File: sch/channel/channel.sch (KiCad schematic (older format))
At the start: 92 parts, among them IC1 STM32F030F4, IC2 L200, IC3 TL072, IC4 LM2594, IC5 TL074, IC6 LM2594, IC7 OPTO_COUPLER, IC8 MCP1700-3002E/TT, P1 CONN_2, P10 CONN_3, P11 CONN_6, P12 CONN_1, P13 CONN_2, P14 CONN_1, P15 CONN_1, P16 CONN_1, P17 CONN_1, P18 CONN_1, P19 CONN_5, P2 CONN_3, P3 DC_JACK, P4 CONN_1, P5 CONN_1, P6 CONN_3, P7 CONN_5, P8 CONN_1, P9 CONN_1, Q1 2N3904, Q2 2N3904, SW1 SWITCH_INV_MECH, SW2 SWITCH_INV_MECH, U1 LM7812

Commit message: Started assigning footprints for components
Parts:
- added C16, C18: 4.7uF, symbol C
- added C17: 1uF, symbol C
- added C19, C20: 100nF, symbol C
- added IC10: 74HCT125, symbol 74HCT125
- added IC9: MCP1824ST-3302E, symbol MCP1824ST-3302E
- added P20, P21: CONN_3, symbol CONN_3
- added P22, P23, P24, P25: CONN_1, symbol CONN_1
- C13: value C -> 100nF
- C7: value C -> 10nF
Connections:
- net +3.3V: now also C17.1, C18.1, IC9.3 (Vout), P20.1 (P1), P21.1 (P1); no longer C10.1, IC6.4 (FB), L2.2, P19.1
- net GND: now also C16.2, C17.2, C18.2, C19.2, IC10.1 (E), IC10.10 (E), IC10.12 (D), IC10.13 (E), IC10.4 (E), IC10.7 (GND), IC10.7 (GND), IC10.7 (GND), IC10.7 (GND), IC9.2 (GND), IC9.4 (GND)
- net ICUR_MEAS: now also C20.1
- net LOAD: now also IC10.2 (D); no longer P19.2
- net SCK: now also IC10.5 (D); no longer P19.3
- net SDO: now also IC10.9 (D); no longer P19.4
- net at IC5.12 (+), R26.2, RV5.1: now also C19.1
- net at IC5.13 (-), R25.2, R28.1: now also C20.2
- new net: P19.1, P21.2 (PM)
- new net: IC10.3 (O), P19.2
- new net: IC10.6 (O), P19.3
- new net: IC10.8 (O), P19.4
- new net +5V: C10.1, C16.1, IC6.4 (FB), IC9.1 (Vin), L2.2, P20.3 (P3), P21.3 (P3)
- new net VCC: IC10.14 (VCC), IC10.14 (VCC), IC10.14 (VCC), IC10.14 (VCC), P20.2 (PM)
- no-connect marks 16 -> 22
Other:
- moved on the sheet: P15, P16, P17, P18, P19

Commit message: Associating some more footprints
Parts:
- removed Q1, Q2: 2N3904, symbol 2N3904
- added Q1, Q2: BC817, symbol BC817
- C12, C14: value C -> 100nF
- C15: value CAPAPOL -> 10uF
- C9: value CAPAPOL -> 1000uF
- D4: value DIODE -> 1N4001
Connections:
- net GND: now also Q2.2 (E)
- net OUT_ON: now also Q2.3 (C)
- net at IC7.2 (K), P2.1 (P1): now also Q1.2 (E)
- net at D4.1 (A), JP7.1, RL1.1: now also Q1.3 (C)
- net at R30.2: now also Q1.1 (B)
- net at R11.1, R12.1: now also Q2.1 (B)
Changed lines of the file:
@@
 LIBS:valves
 LIBS:xilinx
+LIBS:channel-cache
 EELAYER 24 0
 EELAYER END
@@
 $EndComp
 $Comp
-L 2N3904 Q1
-U 1 1 52E5661F
-P 9450 4500
-F 0 "Q1" H 9550 4650 60  0000 C CNN
-F 1 "2N3904" H 9700 4300 60  0000 C CNN
-F 2 "" H 9450 4500 60  0000 C CNN
-F 3 "" H 9450 4500 60  0000 C CNN
-	1    9450 4500
-	-1   0    0    -1
-$EndComp
-$Comp
 L DIODE D4
 U 1 1 52E56633
 P 9000 4050
 F 0 "D4" H 9000 4150 40  0000 C CNN
-F 1 "DIODE" H 9000 3950 40  0000 C CNN
+F 1 "1N4001" H 9000 3950 40  0000 C CNN
 F 2 "" H 9000 4050 60  0000 C CNN
 F 3 "" H 9000 4050 60  0000 C CNN
@@
 P 5500 6550
 F 0 "C12" H 5550 6650 50  0000 L CNN
-F 1 "C" H 5550 6450 50  0000 L CNN
+F 1 "100nF" H 5550 6450 50  0000 L CNN
 F 2 "" H 5500 6550 60  0000 C CNN
 F 3 "" H 5500 6550 60  0000 C CNN
@@
 P 9100 6800
 F 0 "C14" H 9150 6900 50  0000 L CNN
-F 1 "C" H 9150 6700 50  0000 L CNN
+F 1 "100nF" H 9150 6700 50  0000 L CNN
 F 2 "" H 9100 6800 60  0000 C CNN
 F 3 "" H 9100 6800 60  0000 C CNN
@@
 P 10100 6800
 F 0 "C15" H 10150 6900 50  0000 L CNN
-F 1 "CAPAPOL" H 10150 6700 50  0000 L CNN
+F 1 "10uF" H 10150 6700 50  0000 L CNN
 F 2 "" H 10100 6800 60  0000 C CNN
 F 3 "" H 10100 6800 60  0000 C CNN
@@
 Wire Wire Line
 	10050 4050 10050 4150
-$Comp
-L 2N3904 Q2
-U 1 1 536919B5
-P 13200 6600
-F 0 "Q2" H 13300 6750 60  0000 C CNN
-F 1 "2N3904" H 13450 6400 60  0000 C CNN
-F 2 "" H 13200 6600 60  0000 C CNN
-F 3 "" H 13200 6600 60  0000 C CNN
-	1    13200 6600
-	-1   0    0    -1
-$EndComp
 Connection ~ 12050 6600
 Wire Wire Line
@@
 P 2450 1900
 F 0 "C9" H 2500 2000 50  0000 L CNN
-F 1 "CAPAPOL" H 2500 1800 50  0000 L CNN
+F 1 "1000uF" H 2500 1800 50  0000 L CNN
 F 2 "" H 2450 1900 60  0000 C CNN
 F 3 "" H 2450 1900 60  0000 C CNN
@@
 	1    0    0    -1
 $EndComp
+$Comp
+L BC817 Q1
+U 1 1 536C2B82
+P 9450 4500
+F 0 "Q1" H 9550 4650 60  0000 C CNN
+F 1 "BC817" H 9700 4300 60  0000 C CNN
+F 2 "" H 9450 4500 60  0000 C CNN
+F 3 "" H 9450 4500 60  0000 C CNN
+	1    9450 4500
+	-1   0    0    -1
+$EndComp
+$Comp
+L BC817 Q2
+U 1 1 536C363A
+P 13200 6600
+F 0 "Q2" H 13300 6750 60  0000 C CNN
+F 1 "BC817" H 13450 6400 60  0000 C CNN
+F 2 "" H 13200 6600 60  0000 C CNN
+F 3 "" H 13200 6600 60  0000 C CNN
+	1    13200 6600
+	-1   0    0    -1
+$EndComp
 $EndSCHEMATC

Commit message: Fully assigned components, changed the design to remove opto-coupler, using relay instead
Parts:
- removed C14: 100nF, symbol C
- removed C15: 10uF, symbol CAPAPOL
- removed IC7: OPTO_COUPLER, symbol OPTO_COUPLER
- removed Q2: BC817, symbol BC817
- removed R12, R31: 10k, symbol R
- removed R29: 330, symbol R
- removed RL1: RELAY, symbol RELAY
- removed SW2: SWITCH_INV_MECH, symbol SWITCH_INV_MECH
- removed U1: LM7812, symbol LM7812
- added JP11: JUMPER, symbol JUMPER
- added RL1: RELAY_DPDT, symbol RELAY_DPDT
- added SW2: DUAL_SWITCH_INV, symbol DUAL_SWITCH_INV
- L2: value 100uH -> 220uH
- R10: value 1k -> 180
- R11: value 1k -> 10k
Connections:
- net +3.3V: now also RL1.1NO
- net +5V: now also JP11.2
- net GND: now also RL1.1NC
- net OUT_ON: now also D9.1 (A), R11.2, RL1.1C; no longer IC1.9 (PA3/USART1_RX/ADC_IN3)
- net at C11.1, D5.2 (K), IC5.3 (+)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: now also RL1.2C
- net at P2.2 (PM), R30.1: now also SW2.2 (B)
- net at P2.1 (P1), Q1.2 (E): now also JP7.1
- net at D4.1 (A), Q1.3 (C): now also RL1.A1; no longer JP7.1
- net at D4.2 (K), P2.3 (P3): now also JP11.1, RL1.A2, SW2.3 (C); no longer D9.1 (A), R11.2
- net at P12.1, P13.1 (P1): now also RL1.2NO
- net at R11.1: now also IC1.9 (PA3/USART1_RX/ADC_IN3)
- no-connect marks 22 -> 23
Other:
- moved on the sheet: C1, C3, D4, D9, IC8, JP7, P12, P13, P14, P2, Q1, R10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

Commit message: Fully laid out PCB.  Needs a bit of tweaking for optimisation, and silk screen isn't done yet.
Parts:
- removed P20, P21: CONN_3, symbol CONN_3
- removed P22, P23, P24, P25: CONN_1, symbol CONN_1
- removed RV2, RV4: 10k, symbol POT
- added JP12, JP13, JP14, JP15, JP16, JP17: JUMPER, symbol JUMPER
- added RV2, RV4: 10k, symbol POT_MECH
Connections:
- net +3.0VA: now also RV2.3
- net +3.3V: now also RL1.2NO, JP14.2, JP16.2; no longer C1.1, IC8.3 (VIN), RL1.1NO
- net +5V: now also C1.1, IC8.3 (VIN), JP12.1, JP12.2, JP13.1, JP15.1
- net +VIN: now also JP17.2
- net GND: now also IC10.1 (E), IC10.10 (E), IC10.13 (E), IC10.2 (D), IC10.4 (E), P6.1 (P1), RL1.2NC, RV2.1, RV2.GND, RV4.GND; no longer IC10.1 (E), IC10.10 (E), IC10.12 (D), IC10.13 (E), IC10.4 (E), P6.3 (P3), RL1.1NC
- net LOAD: now also IC10.12 (D); no longer IC10.2 (D)
- net OUT_ON: now also RL1.2C; no longer RL1.1C
- net SCK: now also IC10.9 (D); no longer IC10.5 (D)
- net SDO: now also IC10.5 (D); no longer IC10.9 (D)
- net VCC: now also JP13.2, JP14.1
- net at C12.2, D7.2 (K), IC2.4 (REF)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: now also P6.3 (P3), RV4.1; no longer P6.2 (PM)
- net OUT_SENSE: now reaches IC2.5 (OUT), IC5.5 (+), JP3.1, JP3.2, R3.1, R5.1
- net OUT: now reaches C11.1, D5.2 (K), IC5.3 (+), JP6.1, JP6.2, R5.2, R7.1, RV1.3
- net OUT: now also RL1.1C; no longer RL1.2C
- net at RV1.2: now also P6.2 (PM), RV4.2; no longer P6.1 (P1)
- net NEG3V3IN: now reaches C4.1, C5.1, D1.2 (K), IC4.7 (VIN)
- net NEG3V3_SW: now reaches D2.2 (K), IC4.8 (OUT), L1.1
- net 5V_SW: now reaches D6.2 (K), IC6.8 (OUT), L2.1
- net A1: now reaches D4.1 (A), Q1.3 (C), RL1.A1
- net A2: now reaches D4.2 (K), JP11.1, P2.3 (P3), RL1.A2
- net A2: now also SW2.2 (B); no longer SW2.3 (C)
- net RELAY_GND: now reaches JP7.1, P2.1 (P1), Q1.2 (E)
- net at P2.2 (PM), R30.1: now also SW2.3 (C); no longer SW2.2 (B)
- net LED_PWR: now reaches P19.1
- net LED_PWR: now also JP15.2, JP16.1
- net at P19.2: now also IC10.11 (O); no longer IC10.3 (O)
- net at P19.3: now also IC10.8 (O); no longer IC10.6 (O)
- net at P19.4: now also IC10.6 (O); no longer IC10.8 (O)
- net VIN_SW: now reaches C9.1, JP5.1, P1.1 (P1), P3.1 (TIP), SW1.2
- net VIN_SW: now also JP17.1
- net SWITCHED_OUT: now reaches P12.1, P13.1 (P1)
- net SWITCHED_OUT: now also RL1.1NO; no longer RL1.2NO
- net at C12.1, IC3.2 (-), IC3.5 (+)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: now also RV2.2
- no-connect marks 23 -> 19
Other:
- note added: "0805 0Ohm link rated at 2A, so doubling up for safety"
- moved on the sheet: C1, C16, C17, C3, D4, IC8, IC9, JP10, JP11, JP7, JP8, JP9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

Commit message: A few tweaks to improve the layout.  Still not sorted silk screen.
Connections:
- net LOAD: now also IC1.14 (PB1/ADC_IN9); no longer IC1.10 (PA4/SPI1_NSS/USART1_CK/ADC_IN4)
- net at P8.1: now also IC1.10 (PA4/SPI1_NSS/USART1_CK/ADC_IN4); no longer IC1.14 (PB1/ADC_IN9)
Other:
- moved on the sheet: C7, JP2, P8, R1
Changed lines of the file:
@@
 Connection ~ 14000 4300
 Wire Wire Line
-	13400 4300 13200 4300
+	13200 4300 13400 4300
 Wire Wire Line
 	13300 4300 13300 4100
@@
 	12600 4300 12600 4100
 Wire Wire Line
-	12600 3700 12600 3450
+	12600 3450 12600 3700
 Wire Wire Line
 	12100 3450 12750 3450
@@
 Connection ~ 6950 2500
 Wire Wire Line
-	6500 1300 6000 1300
-Wire Wire Line
-	7000 1300 7850 1300
+	6000 1300 6500 1300
+Wire Wire Line
+	7850 1300 7000 1300
 Wire Wire Line
 	7850 700  7850 1900
@@
 Connection ~ 7700 2500
 Wire Wire Line
-	7100 2500 6800 2500
+	6800 2500 7100 2500
 Wire Wire Line
 	8100 1000 7850 1000
@@
 	3350 1200 5000 1200
 Wire Wire Line
-	14550 1650 14150 1650
+	14150 1650 14550 1650
 Wire Wire Line
 	14350 1800 14350 1650
@@
 	10200 3500 10300 3500
 Wire Wire Line
-	10300 3300 9300 3300
+	9300 3300 10300 3300
 Wire Wire Line
 	9400 4750 9400 4850
@@
 	7250 6400 7250 6600
 Wire Wire Line
-	7100 6850 6850 6850
+	6850 6850 7100 6850
 Wire Wire Line
 	6850 6550 6850 7150
@@
 Text Label 6100 10400 2    60   ~ 0
 SDO
-Text Label 2000 10600 0    60   ~ 0
+Text Label 6100 10300 2    60   ~ 0
 LOAD
 Wire Wire Line
@@
 	1500 9350 1500 9450
 Wire Wire Line
-	5700 10100 6550 10100
-Wire Wire Line
-	6550 10100 6550 9150
+	6550 10100 5700 10100
+Wire Wire Line
+	6550 9150 6550 10100
 Wire Wire Line
 	5700 10200 6550 10200
@@
 $EndComp
 Wire Wire Line
-	2300 10100 1000 10100
-Wire Wire Line
-	1000 9300 1000 10200
+	850  10100 2300 10100
+Wire Wire Line
+	850  9300 850  10200
 $Comp
 L C C7
 U 1 1 53685342
-P 1000 10400
-F 0 "C7" H 1050 10500 50  0000 L CNN
-F 1 "10nF" H 1050 10300 50  0000 L CNN
-F 2 "" H 1000 10400 60  0000 C CNN
-F 3 "" H 1000 10400 60  0000 C CNN
-	1    1000 10400
+P 850 10400
+F 0 "C7" H 900 10500 50  0000 L CNN
+F 1 "10nF" H 900 10300 50  0000 L CNN
+F 2 "" H 850 10400 60  0000 C CNN
+F 3 "" H 850 10400 60  0000 C CNN
+	1    850  10400
 	-1   0    0    -1
 $EndComp
 Wire Wire Line
-	1000 10600 1000 10700
-Connection ~ 1000 10100
+	850  10600 850  10700
+Connection ~ 850  10100
 $Comp
 L GND #PWR033
 U 1 1 536856E7
-P 1000 10700
-F 0 "#PWR033" H 1000 10700 30  0001 C CNN
-F 1 "GND" H 1000 10630 30  0001 C CNN
-F 2 "" H 1000 10700 60  0000 C CNN
-F 3 "" H 1000 10700 60  0000 C CNN
-	1    1000 10700
+P 850 10700
+F 0 "#PWR033" H 850 10700 30  0001 C CNN
+F 1 "GND" H 850 10630 30  0001 C CNN
+F 2 "" H 850 10700 60  0000 C CNN
+F 3 "" H 850 10700 60  0000 C CNN
+	1    850  10700
 	1    0    0    -1
 $EndComp
@@
 L +3.0VA #PWR034
 U 1 1 5368574A
-P 1000 9300
-F 0 "#PWR034" H 1000 9260 30  0001 C CNN
-F 1 "+3.0VA" H 1000 9410 30  0000 C CNN
-F 2 "" H 1000 9300 60  0000 C CNN
-F 3 "" H 1000 9300 60  0000 C CNN
-	1    1000 9300
+P 850 9300
+F 0 "#PWR034" H 850 9260 30  0001 C CNN
+F 1 "+3.0VA" H 850 9410 30  0000 C CNN
+F 2 "" H 850 9300 60  0000 C CNN
+F 3 "" H 850 9300 60  0000 C CNN
+	1    850  9300
 	1    0    0    -1
 $EndComp
@@
 $EndComp
 Wire Wire Line
-	2300 10000 1250 10000
-Wire Wire Line
-	1250 9900 1250 10200
-Connection ~ 1250 10000
+	1100 10000 2300 10000
+Wire Wire Line
+	1100 9900 1100 10200
+Connection ~ 1100 10000
 $Comp
 L JUMPER JP2
 U 1 1 5368ABD1
-P 1250 10400
-F 0 "JP2" H 1250 10550 60  0000 C CNN
-F 1 "RESET" H 1250 10320 40  0000 C CNN
-F 2 "" H 1250 10400 60  0000 C CNN
-F 3 "" H 1250 10400 60  0000 C CNN
-	1    1250 10400
+P 1100 10400
+F 0 "JP2" H 1100 10550 60  0000 C CNN
+F 1 "RESET" H 1100 10320 40  0000 C CNN
+F 2 "" H 1100 10400 60  0000 C CNN
+F 3 "" H 1100 10400 60  0000 C CNN
+	1    1100 10400
 	0    1    1    0
 $EndComp
@@
 L GND #PWR039
 U 1 1 5368AC53
-P 1250 10700
-F 0 "#PWR039" H 1250 10700 30  0001 C CNN
-F 1 "GND" H 1250 10630 30  0001 C CNN
-F 2 "" H 1250 10700 60  0000 C CNN
-F 3 "" H 1250 10700 60  0000 C CNN
-	1    1250 10700
+P 1100 10700
+F 0 "#PWR039" H 1100 10700 30  0001 C CNN
+F 1 "GND" H 1100 10630 30  0001 C CNN
+F 2 "" H 1100 10700 60  0000 C CNN
+F 3 "" H 1100 10700 60  0000 C CNN
+	1    1100 10700
 	1    0    0    -1
 $EndComp
@@
 L +3.3V #PWR040
 U 1 1 5368ACA6
-P 1250 9300
-F 0 "#PWR040" H 1250 9260 30  0001 C CNN
-F 1 "+3.3V" H 1250 9410 30  0000 C CNN
-F 2 "" H 1250 9300 60  0000 C CNN
-F 3 "" H 1250 9300 60  0000 C CNN
-	1    1250 9300
+P 1100 9300
+F 0 "#PWR040" H 1100 9260 30  0001 C CNN
+F 1 "+3.3V" H 1100 9410 30  0000 C CNN
+F 2 "" H 1100 9300 60  0000 C CNN
+F 3 "" H 1100 9300 60  0000 C CNN
+	1    1100 9300
 	1    0    0    -1
 $EndComp
@@
 L R R1
 U 1 1 5368ACF9
-P 1250 9650
-F 0 "R1" V 1330 9650 50  0000 C CNN
-F 1 "10k" V 1250 9650 50  0000 C CNN
-F 2 "" H 1250 9650 60  0000 C CNN
-F 3 "" H 1250 9650 60  0000 C CNN
-	1    1250 9650
-	1    0    0    -1
-$EndComp
-Wire Wire Line
-	1250 9400 1250 9300
-Wire Wire Line
-	1250 10600 1250 10700
+P 1100 9650
+F 0 "R1" V 1180 9650 50  0000 C CNN
+F 1 "10k" V 1100 9650 50  0000 C CNN
+F 2 "" H 1100 9650 60  0000 C CNN
+F 3 "" H 1100 9650 60  0000 C CNN
+	1    1100 9650
+	1    0    0    -1
+$EndComp
+Wire Wire Line
+	1100 9400 1100 9300
+Wire Wire Line
+	1100 10600 1100 10700
 Wire Wire Line
 	2650 2400 2650 3400
 Connection ~ 2650 3400
 Wire Wire Line
-	2750 3400 1800 3400
+	1800 3400 2750 3400
 Wire Wire Line
 	3350 1200 3350 3950
@@
 L CONN_1 P8
 U 1 1 536999A7
-P 6350 10300
-F 0 "P8" H 6430 10300 40  0000 C CNN
-F 1 "CONN_1" H 6300 10340 30  0001 C CNN
-F 2 "" H 6350 10300 60  0000 C CNN
-F 3 "" H 6350 10300 60  0000 C CNN
-	1    6350 10300
-	1    0    0    -1
+P 1850 10600
+F 0 "P8" H 1930 10600 40  0000 C CNN
+F 1 "CONN_1" H 1800 10640 30  0001 C CNN
+F 2 "" H 1850 10600 60  0000 C CNN
+F 3 "" H 1850 10600 60  0000 C CNN
+	1    1850 10600
+	-1   0    0    1
 $EndComp
 $Comp
@@
 	2300 9900 1950 9900
 Wire Wire Line
-	5700 10300 6200 10300
+	5700 10300 6100 10300
 Wire Wire Line
 	6200 10500 5700 10500
@@
 $EndComp
 Wire Wire Line
-	1600 7350 1600 7450
+	1600 7450 1600 7350
 Wire Wire Line
 	900  7450 2100 7450
@@
 $EndComp
 Wire Wire Line
-	11000 1400 10100 1400
+	10100 1400 11000 1400
 Wire Wire Line
 	10700 1600 10700 1400
@@
 $EndComp
 Wire Wire Line
-	12450 7300 12800 7300
-Wire Wire Line
-	12800 7300 12800 6500
+	12800 7300 12450 7300
+Wire Wire Line
+	12800 6500 12800 7300
 Wire Wire Line
 	12450 7500 12800 7500

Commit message: Started ripping up the channel board to add a heatsink for standalone mode, and switch the display around so it faces the right way.
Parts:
- added IC7: L200, symbol L200
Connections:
- net +VIN: now also C9.1, IC7.1 (IN)
- net -3.3V: now also IC7.3 (GND)
- net OUT_SENSE: now also IC7.5 (OUT)
- net VIN_SW: no longer C9.1
- net at IC2.2 (LIMIT), R3.2: now also IC7.2 (LIMIT)
- net at C12.2, D7.2 (K), IC2.4 (REF)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: now also IC7.4 (REF)
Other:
- moved on the sheet: C9
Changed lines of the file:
@@
 $EndComp
 Wire Wire Line
-	2550 4500 2450 4500
+	2450 4500 3050 4500
 Wire Wire Line
 	1050 4600 1050 4500
@@
 Connection ~ 2650 3400
 Wire Wire Line
-	1800 3400 2750 3400
+	1000 3400 2750 3400
 Wire Wire Line
 	3350 1200 3350 3950
@@
 	2900 5600 2900 5500
 Wire Wire Line
-	2650 5350 1600 5350
+	500  5350 2650 5350
 $Comp
 L DIODE D5
@@
 Connection ~ 800  4350
 Wire Wire Line
-	1000 3850 1000 3750
-Wire Wire Line
-	1000 3750 800  3750
+	1000 3750 1000 3850
+Wire Wire Line
+	600  3750 1000 3750
 Connection ~ 800  3750
 $Comp
@@
 	12800 6500 12800 7300
 Wire Wire Line
-	12450 7500 12800 7500
-Wire Wire Line
 	12550 7500 12550 7600
 $Comp
@@
 L CAPAPOL C9
 U 1 1 537057C1
-P 13200 7400
-F 0 "C9" H 13250 7500 50  0000 L CNN
-F 1 "1000uF" H 13250 7300 50  0000 L CNN
-F 2 "" H 13200 7400 60  0000 C CNN
-F 3 "" H 13200 7400 60  0000 C CNN
-	1    13200 7400
-	1    0    0    -1
-$EndComp
-Wire Wire Line
-	13200 7200 13200 7100
-Wire Wire Line
-	13200 7100 12800 7100
+P 14650 6900
+F 0 "C9" H 14700 7000 50  0000 L CNN
+F 1 "1000uF" H 14700 6800 50  0000 L CNN
+F 2 "" H 14650 6900 60  0000 C CNN
+F 3 "" H 14650 6900 60  0000 C CNN
+	1    14650 6900
+	1    0    0    -1
+$EndComp
 Connection ~ 12800 7100
-Wire Wire Line
-	13200 7600 13200 7700
-Wire Wire Line
-	13200 7700 12800 7700
-Wire Wire Line
-	12800 7700 12800 7500
-Connection ~ 12550 7500
 $Comp
 L SWITCH_INV_MECH SW1
@@
 	14100 6600 14650 6600
 Wire Wire Line
-	14650 6600 14650 6300
+	14650 6300 14650 6700
 $Comp
 L GND #PWR086
@@
 Wire Wire Line
 	10450 7800 10450 7700
+$Comp
+L L200 IC7
+U 1 1 5377964D
+P 1750 2050
+F 0 "IC7" H 1500 2400 60  0000 C CNN
+F 1 "L200" H 1750 2050 60  0000 C CNN
+F 2 "" H 1750 2050 60  0000 C CNN
+F 3 "" H 1750 2050 60  0000 C CNN
+	1    1750 2050
+	1    0    0    -1
+$EndComp
+Wire Wire Line
+	600  3750 600  2050
+Wire Wire Line
+	600  2050 1100 2050
+Wire Wire Line
+	1000 3400 1000 1300
+Wire Wire Line
+	1000 1300 1750 1300
+Wire Wire Line
+	1750 1300 1750 1450
+Wire Wire Line
+	500  5350 500  2800
+Wire Wire Line
+	500  2800 1550 2800
+Wire Wire Line
+	1550 2800 1550 2650
+Wire Wire Line
+	3050 4500 3050 3750
+Wire Wire Line
+	3050 3750 3550 3750
+Wire Wire Line
+	3550 3750 3550 2050
+Wire Wire Line
+	3550 2050 2400 2050
+Connection ~ 2550 4500
+Wire Wire Line
+	2900 5150 2900 4350
+Wire Wire Line
+	2900 4350 2300 4350
+Wire Wire Line
+	2300 4350 2300 3650
+Wire Wire Line
+	2300 3650 1450 3650
+Wire Wire Line
+	1450 3650 1450 2900
+Wire Wire Line
+	1450 2900 1950 2900
+Wire Wire Line
+	1950 2900 1950 2650
+Connection ~ 2900 5150
+Wire Wire Line
+	12550 7500 12450 7500
+Connection ~ 14650 6600
+Wire Wire Line
+	14650 7100 14650 7200
+$Comp
+L GND #PWR?
+U 1 1 5377A578
+P 14650 7200
+F 0 "#PWR?" H 14650 7200 30  0001 C CNN
+F 1 "GND" H 14650 7130 30  0001 C CNN
+F 2 "" H 14650 7200 60  0000 C CNN
+F 3 "" H 14650 7200 60  0000 C CNN
+	1    14650 7200
+	1    0    0    -1
+$EndComp
 $EndSCHEMATC

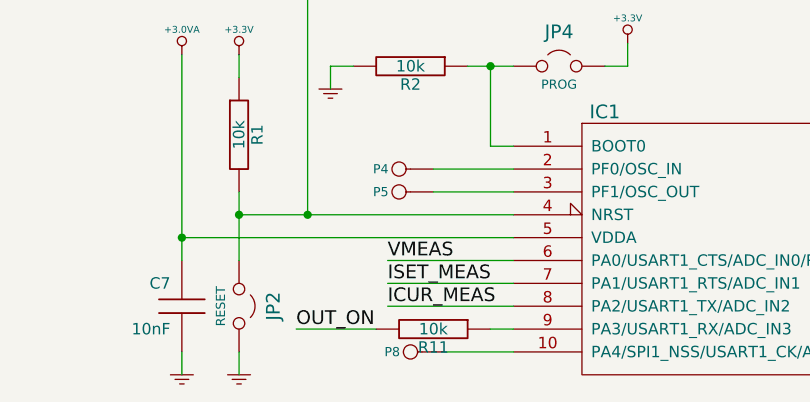
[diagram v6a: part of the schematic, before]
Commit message: More or less happy with the channel PCB.  Needs silk screen sorting out.
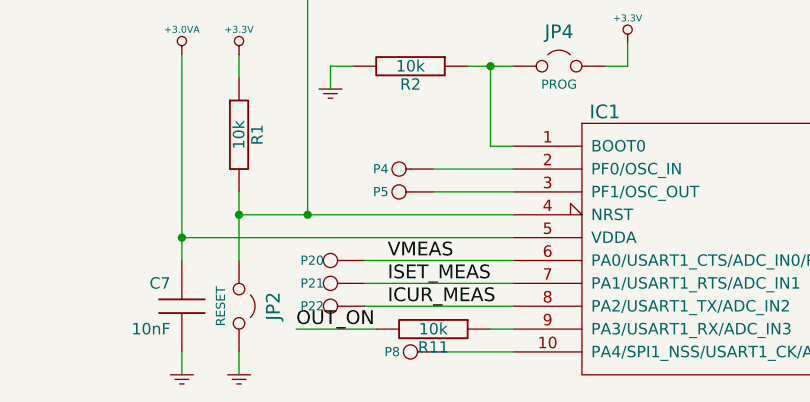
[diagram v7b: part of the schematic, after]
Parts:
- added P20, P21, P22: CONN_1, symbol CONN_1
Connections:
- net ICUR_MEAS: now also P22.1
- net ISET_MEAS: now also P21.1
- net VMEAS: now also P20.1

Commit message: Final changes before ordering PCBs
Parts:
- JP1: value JUMPER -> VIN
- JP10: value JUMPER -> GND
- JP12: value JUMPER -> 5V
- JP3: value JUMPER -> OUT_SENSE
- JP6: value JUMPER -> OUT
- JP8: value JUMPER -> 3.3V
- JP9: value JUMPER -> -3.3V
- P1: value CONN_2 -> 17-24VDC
- P10: value CONN_3 -> CURRENT
- P11: value CONN_6 -> FTDI
- P13: value CONN_2 -> OUTPUT
- P19: value CONN_5 -> LED_DISPLAY
- P2: value CONN_3 -> OUT_ON
- P20: value CONN_1 -> V
- P21: value CONN_1 -> I_SET
- P22: value CONN_1 -> I_NOW
- P3: value DC_JACK -> 17-24VDC PIN +VE
- P6: value CONN_3 -> VOLTAGE
- P7: value CONN_5 -> SWD
- SW2: value DUAL_SWITCH_INV -> OUT_ON
